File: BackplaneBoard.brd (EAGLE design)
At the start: 139.7 x 76.2 mm, 17 parts

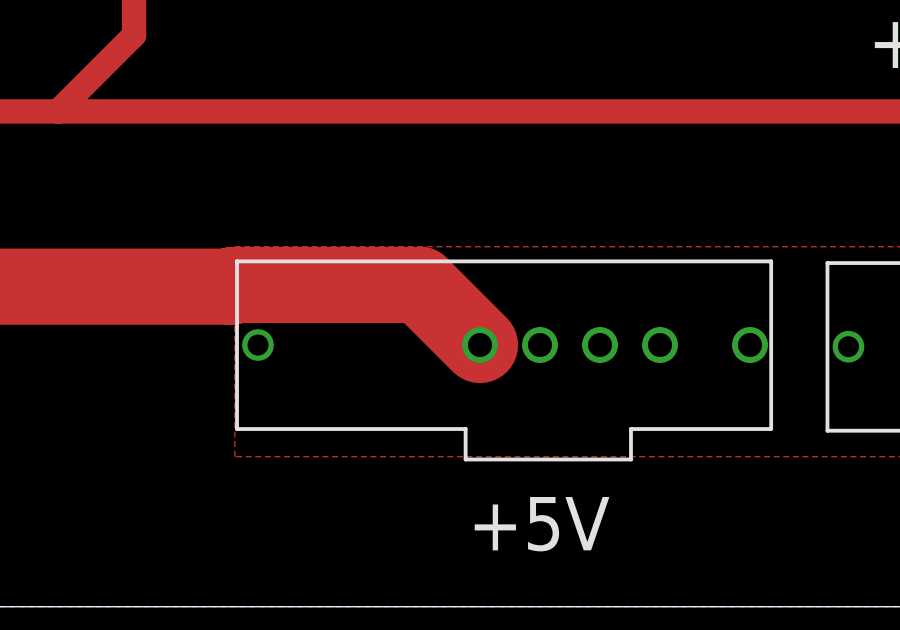
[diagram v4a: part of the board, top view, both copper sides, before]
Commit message: Small routing changes
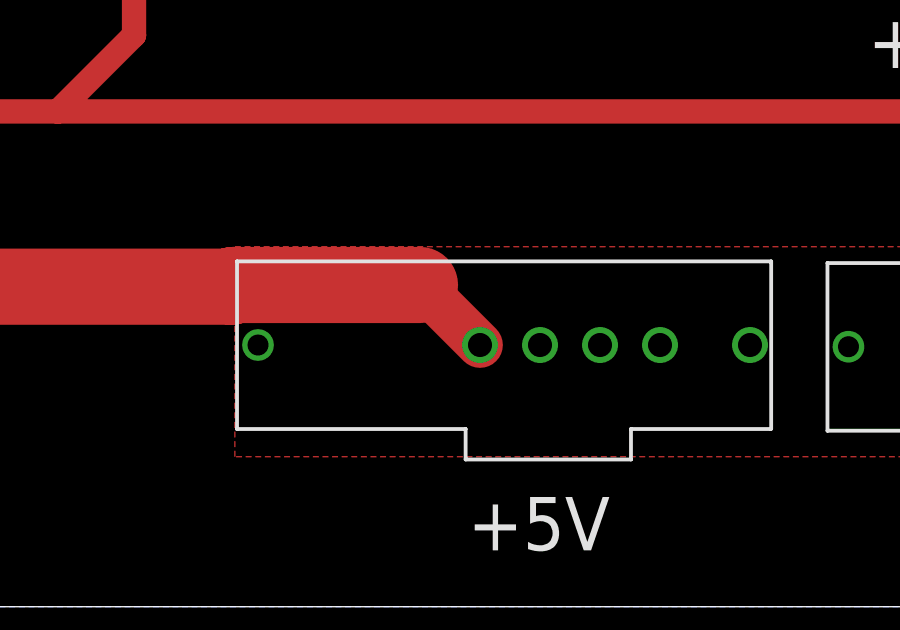
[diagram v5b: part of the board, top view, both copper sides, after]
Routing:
- net +5V: track 91.3 -> 88.1 mm
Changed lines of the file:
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@@
 <vertex x="82" y="5"/>
 </polygon>
-<wire x1="49.8962" y1="11" x2="52.1724" y2="8.7238" width="1.27" layer="1"/>
 <wire x1="7.32" y1="46.99" x2="4.3434" y2="46.99" width="2.54" layer="1"/>
 <wire x1="4.3434" y1="46.99" x2="3.302" y2="45.9486" width="2.54" layer="1"/>
@@
 <wire x1="43.88675625" y1="10.668" x2="43.94355625" y2="10.7248" width="2.54" layer="1"/>
 <wire x1="43.94355625" y1="10.7248" x2="50.1714" y2="10.7248" width="2.54" layer="1"/>
-<wire x1="50.1714" y1="10.7248" x2="52.1724" y2="8.7238" width="2.54" layer="1"/>
+<wire x1="50.1714" y1="10.7248" x2="52.1724" y2="8.7238" width="1.524" layer="1"/>
 </signal>
 </signals>

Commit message: Final Board
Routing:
- net CAN_L: track 225.8 -> 184.4 mm
- net CAN_H: track 217.6 -> 183.6 mm
- net +3V3: track 129.7 -> 127.7 mm
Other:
- board text added: "Backplane v1 Melchor De La Garza Cynthia Zatlokowicz Jacob Bobson"
